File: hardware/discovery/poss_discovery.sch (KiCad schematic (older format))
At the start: 56 parts, among them J1 HEADER_2, J2 HEADER_25x2, J3 HEADER_25x2, J5 HEADER_2, SW1 SW_PUSH, SW10 SW_PUSH, SW11 SW_PUSH, SW12 SW_PUSH, SW13 SW_PUSH, SW14 SW_PUSH, SW15 SW_PUSH, SW16 SW_PUSH, SW17 SW_PUSH, SW18 SW_PUSH, SW19 SW_PUSH, SW2 SW_PUSH, SW20 SW_PUSH, SW21 SW_PUSH, SW22 SW_PUSH, SW3 SW_PUSH, SW4 SW_PUSH, SW5 SW_PUSH, SW6 SW_PUSH, SW7 SW_PUSH, SW8 SW_PUSH, SW9 SW_PUSH

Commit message: Start RevB of the discovery board
- Fix RevA known problems
- Custom scheme and footprint for the headers
- Improved silkscreen
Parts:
- removed J1, J5: HEADER_2, Pin_Headers:Pin_Header_Straight_2x01, symbol HEADER_2
- removed J2, J3: HEADER_25x2, Pin_Headers:Pin_Header_Straight_2x25, symbol HEADER_25x2
- added U1: STM32F4_DISCO_Header, stm32f4-disco:STM32F4-DISCO-HEADERS-TH, symbol STM32F4_DISCO_Header
- RV1, RV2: symbol POT -> POT-RESCUE-poss_discovery
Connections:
- net labels added: BA, BB, BC, BD, BE, BPM_VOL, DISCO_USER_BTN, STM_LED1, SWDCLK, SWDIO, USB_Over_Current, VBUS_FS
- net labels removed: 5V, BOOT0, BP7, BPM, NC, NRTS, PA0, PA1, PA10, PA13, PA14, PA15, PA2, PA3, PA4, PA5, PA6, PA7, PA8, PA9, PB0, PB1, PB10, PB11, PB12, PB13, PB14, PB15, PB2, PB3, PB4, PB5, PB6, PB8, PB9, PC0, PC1, PC10, PC11, PC12, PC13, PC14, PC15, PC2, PC3, PC4, PC5, PC6, PC7, PC8, PC9, PD0, PD1, PD10, PD11, PD12, PD13, PD14, PD15, PD2, PD3, PD4, PD5, PD6, PD7, PD8, PD9, PE0, PE1, PE10, PE11, PE12, PE13, PE14, PE15, PE2, PE3, PE4, PE5, PE6, PE7, PE8, PE9, PH0, PH1, STM_LED_1, STM_USER_BTN, USB_Over_I, VDD, VDD2, Vbus_FS
- wire segments 173 -> 44

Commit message: Discovery: Start power section
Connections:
- net 3V renamed 3V3
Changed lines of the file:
@@
 LIBS:w_connectors
 LIBS:stm32f4_disco_header
+LIBS:74xgxx
+LIBS:ac-dc
+LIBS:brooktre
+LIBS:cmos_ieee
+LIBS:dc-dc
+LIBS:elec-unifil
+LIBS:ftdi
+LIBS:gennum
+LIBS:graphic
+LIBS:logo
+LIBS:microchip_pic10mcu
+LIBS:microchip_pic12mcu
+LIBS:microchip_pic16mcu
+LIBS:microchip1
+LIBS:msp430
+LIBS:nxp_armmcu
+LIBS:powerint
+LIBS:pspice
+LIBS:references
+LIBS:relays
+LIBS:sensors
+LIBS:special
+LIBS:stm8
+LIBS:stm32
+LIBS:supertex
+LIBS:transf
+LIBS:ttl_ieee
+LIBS:video
 LIBS:poss_discovery-cache
 EELAYER 25 0
@@
 $Descr A4 11693 8268
 encoding utf-8
-Sheet 1 1
+Sheet 1 3
 Title "Pocket Open Source Syntesizer - Discovery"
 Date ""
@@
 $EndComp
 Wire Wire Line
-	7400 750  7400 3500
+	7400 750  7400 3750
 Connection ~ 7400 3150
 Connection ~ 7400 2800
@@
 Connection ~ 7400 1100
 Wire Wire Line
-	8650 750  8650 3500
+	8650 750  8650 3750
 Connection ~ 8650 3150
 Connection ~ 8650 2800
@@
 Text GLabel 2200 4950 2    60   Input ~ 0
 GND
-Text GLabel 5350 4950 2    60   Input ~ 0
-GND
 Text GLabel 5350 1350 2    60   Input ~ 0
 GND
@@
 ROW5
 Text GLabel 5350 1650 2    60   Input ~ 0
-3V
+3V3
 Text GLabel 4400 1650 0    60   Input ~ 0
-3V
+3V3
 Text GLabel 3350 5650 2    60   Input ~ 0
 POT1
 Text GLabel 4700 5650 2    60   Input ~ 0
 POT2
-Text GLabel 4950 5900 2    60   Input ~ 0
-GND
-Text GLabel 3600 5900 2    60   Input ~ 0
-GND
 Text GLabel 3100 5900 0    60   Input ~ 0
-3V
+3V3
 Text GLabel 4450 5900 0    60   Input ~ 0
-3V
-Text GLabel 9950 3500 2    60   Input ~ 0
-GND
-Text GLabel 8650 3500 2    60   Input ~ 0
-GND
-Text GLabel 7400 3500 2    60   Input ~ 0
-GND
+3V3
 $Comp
 L GND #PWR01
@@
 Text GLabel 2200 1350 2    60   Input ~ 0
 GND
+$Sheet
+S 1550 6600 1350 1100
+U 585D2CBE
+F0 "Power" 60
+F1 "power.sch" 60
+$EndSheet
+$Comp
+L GND #PWR?
+U 1 1 585D97BE
+P 8650 3750
+F 0 "#PWR?" H 8650 3750 30  0001 C CNN
+F 1 "GND" H 8650 3680 30  0001 C CNN
+F 2 "" H 8650 3750 60  0001 C CNN
+F 3 "" H 8650 3750 60  0001 C CNN
+	1    8650 3750
+	1    0    0    -1
+$EndComp
+Connection ~ 8650 3500
+$Comp
+L GND #PWR?
+U 1 1 585D9E6B
+P 7400 3750
+F 0 "#PWR?" H 7400 3750 30  0001 C CNN
+F 1 "GND" H 7400 3680 30  0001 C CNN
+F 2 "" H 7400 3750 60  0001 C CNN
+F 3 "" H 7400 3750 60  0001 C CNN
+	1    7400 3750
+	1    0    0    -1
+$EndComp
+Connection ~ 7400 3500
+$Comp
+L GND #PWR?
+U 1 1 585DAFE1
+P 4950 6000
+F 0 "#PWR?" H 4950 6000 30  0001 C CNN
+F 1 "GND" H 4950 5930 30  0001 C CNN
+F 2 "" H 4950 6000 60  0001 C CNN
+F 3 "" H 4950 6000 60  0001 C CNN
+	1    4950 6000
+	1    0    0    -1
+$EndComp
+$Comp
+L GND #PWR?
+U 1 1 585DB05F
+P 3600 6000
+F 0 "#PWR?" H 3600 6000 30  0001 C CNN
+F 1 "GND" H 3600 5930 30  0001 C CNN
+F 2 "" H 3600 6000 60  0001 C CNN
+F 3 "" H 3600 6000 60  0001 C CNN
+	1    3600 6000
+	1    0    0    -1
+$EndComp
+Wire Wire Line
+	3600 5900 3600 6000
+Wire Wire Line
+	4950 5900 4950 6000
+Wire Wire Line
+	5350 4950 5500 4950
+Wire Wire Line
+	5500 4950 5500 5100
+Text GLabel 5500 4950 2    60   Input ~ 0
+GND
+$Comp
+L GND #PWR?
+U 1 1 585DBA46
+P 5500 5100
+F 0 "#PWR?" H 5500 5100 30  0001 C CNN
+F 1 "GND" H 5500 5030 30  0001 C CNN
+F 2 "" H 5500 5100 60  0001 C CNN
+F 3 "" H 5500 5100 60  0001 C CNN
+	1    5500 5100
+	1    0    0    -1
+$EndComp
+$Sheet
+S 3200 6600 1400 1100
+U 585DBE08
+F0 "Micro-Controller" 60
+F1 "micro-controller.sch" 60
+$EndSheet
 $EndSCHEMATC

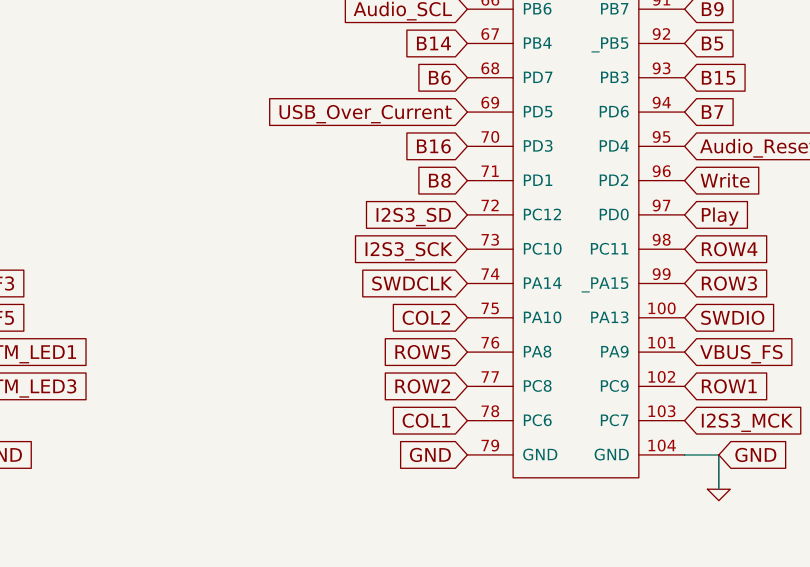
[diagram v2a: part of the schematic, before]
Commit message: Discovery: add the MCU
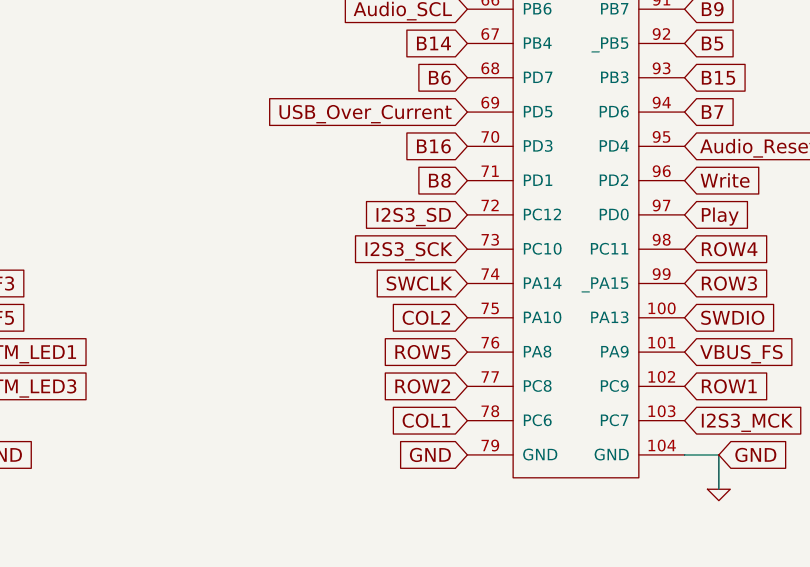
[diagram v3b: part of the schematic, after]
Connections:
- net SWDCLK renamed SWCLK
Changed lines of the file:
@@
 COL2
 Text GLabel 4400 4200 0    60   Input ~ 0
-SWDCLK
+SWCLK
 Text GLabel 4400 4050 0    60   Input ~ 0
 I2S3_SCK

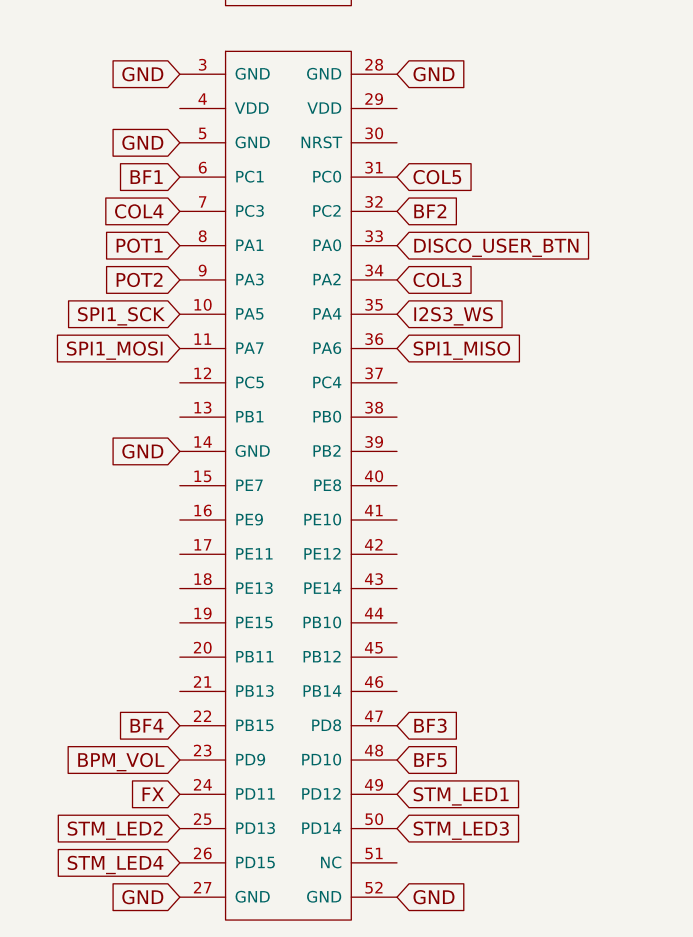
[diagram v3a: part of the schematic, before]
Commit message: Discovery: Fix channel button labels
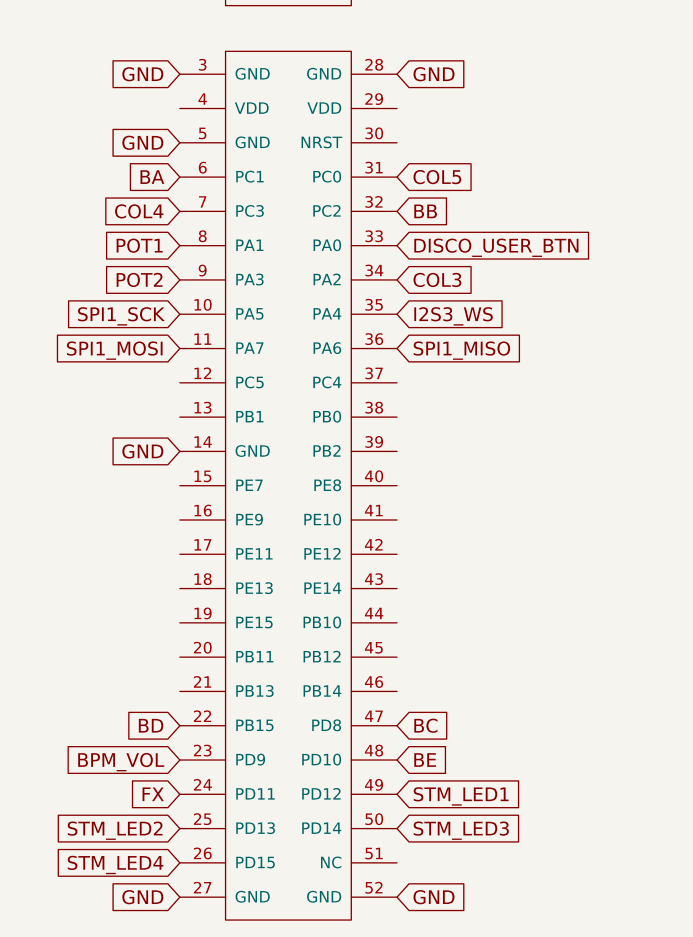
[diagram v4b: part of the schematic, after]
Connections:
- net BF1 is gone; now on net BA: U1.6 (PC1)
- net BF2 is gone; now on net BB: U1.32 (PC2)
- net BF3 is gone; now on net BC: U1.47 (PD8)
- net BF4 is gone; now on net BD: U1.22 (PB15)
- net BF5 is gone; now on net BE: U1.48 (PD10)
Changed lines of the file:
@@
 $EndComp
 Text GLabel 1250 1800 0    60   Input ~ 0
-BF1
+BA
 Text GLabel 1250 1950 0    60   Input ~ 0
 COL4
@@
 COL5
 Text GLabel 2200 1950 2    60   Input ~ 0
-BF2
+BB
 Text GLabel 2200 2100 2    60   Input ~ 0
 DISCO_USER_BTN
@@
 BPM_VOL
 Text GLabel 1250 4200 0    60   Input ~ 0
-BF4
+BD
 Text GLabel 2200 4650 2    60   Input ~ 0
 STM_LED3
@@
 STM_LED1
 Text GLabel 2200 4350 2    60   Input ~ 0
-BF5
+BE
 Text GLabel 2200 4200 2    60   Input ~ 0
-BF3
+BC
 Text GLabel 5350 4800 2    60   Input ~ 0
 I2S3_MCK
@@
 $EndSheet
 $Comp
-L GND #PWR?
+L GND #PWR02
 U 1 1 585D97BE
 P 8650 3750
-F 0 "#PWR?" H 8650 3750 30  0001 C CNN
+F 0 "#PWR02" H 8650 3750 30  0001 C CNN
 F 1 "GND" H 8650 3680 30  0001 C CNN
 F 2 "" H 8650 3750 60  0001 C CNN
@@
 Connection ~ 8650 3500
 $Comp
-L GND #PWR?
+L GND #PWR03
 U 1 1 585D9E6B
 P 7400 3750
-F 0 "#PWR?" H 7400 3750 30  0001 C CNN
+F 0 "#PWR03" H 7400 3750 30  0001 C CNN
 F 1 "GND" H 7400 3680 30  0001 C CNN
 F 2 "" H 7400 3750 60  0001 C CNN
@@
 Connection ~ 7400 3500
 $Comp
-L GND #PWR?
+L GND #PWR04
 U 1 1 585DAFE1
 P 4950 6000
-F 0 "#PWR?" H 4950 6000 30  0001 C CNN
+F 0 "#PWR04" H 4950 6000 30  0001 C CNN
 F 1 "GND" H 4950 5930 30  0001 C CNN
 F 2 "" H 4950 6000 60  0001 C CNN
@@
 $EndComp
 $Comp
-L GND #PWR?
+L GND #PWR05
 U 1 1 585DB05F
 P 3600 6000
-F 0 "#PWR?" H 3600 6000 30  0001 C CNN
+F 0 "#PWR05" H 3600 6000 30  0001 C CNN
 F 1 "GND" H 3600 5930 30  0001 C CNN
 F 2 "" H 3600 6000 60  0001 C CNN
@@
 GND
 $Comp
-L GND #PWR?
+L GND #PWR06
 U 1 1 585DBA46
 P 5500 5100
-F 0 "#PWR?" H 5500 5100 30  0001 C CNN
+F 0 "#PWR06" H 5500 5100 30  0001 C CNN
 F 1 "GND" H 5500 5030 30  0001 C CNN
 F 2 "" H 5500 5100 60  0001 C CNN

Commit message: Discovery start power section
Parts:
- U1: footprint stm32f4-disco:STM32F4-DISCO-HEADERS-TH -> stm32f4-disco:STM32F4-DISCO-HEADERS-SMD
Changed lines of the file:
@@
 LIBS:contrib
 LIBS:valves
-LIBS:w_connectors
 LIBS:stm32f4_disco_header
 LIBS:74xgxx
@@
 F 0 "U1" H 1550 5200 60  0000 C CNN
 F 1 "STM32F4_DISCO_Header" H 2000 5050 60  0000 C CNN
-F 2 "stm32f4-disco:STM32F4-DISCO-HEADERS-TH" H 3350 2900 60  0001 C CNN
+F 2 "stm32f4-disco:STM32F4-DISCO-HEADERS-SMD" H 3350 2900 60  0001 C CNN
 F 3 "" H 3350 2900 60  0001 C CNN
 	1    3350 2900

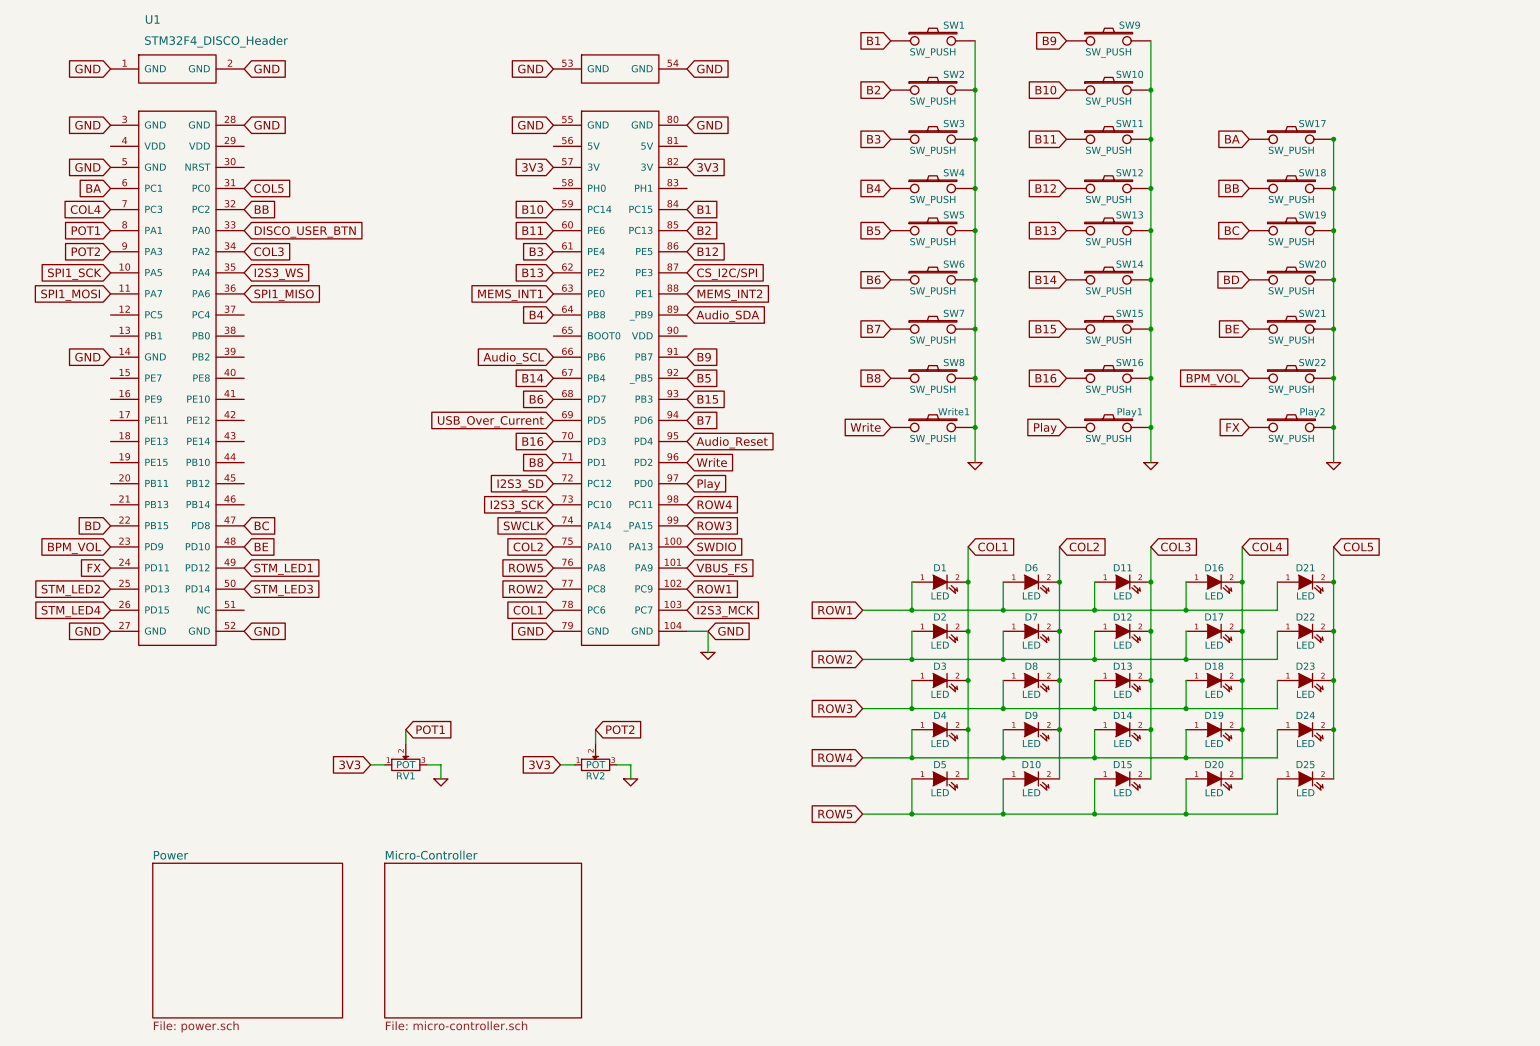
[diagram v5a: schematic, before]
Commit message: Discovery: switch to a 9x3 LED matrix to simplify the PCB layout
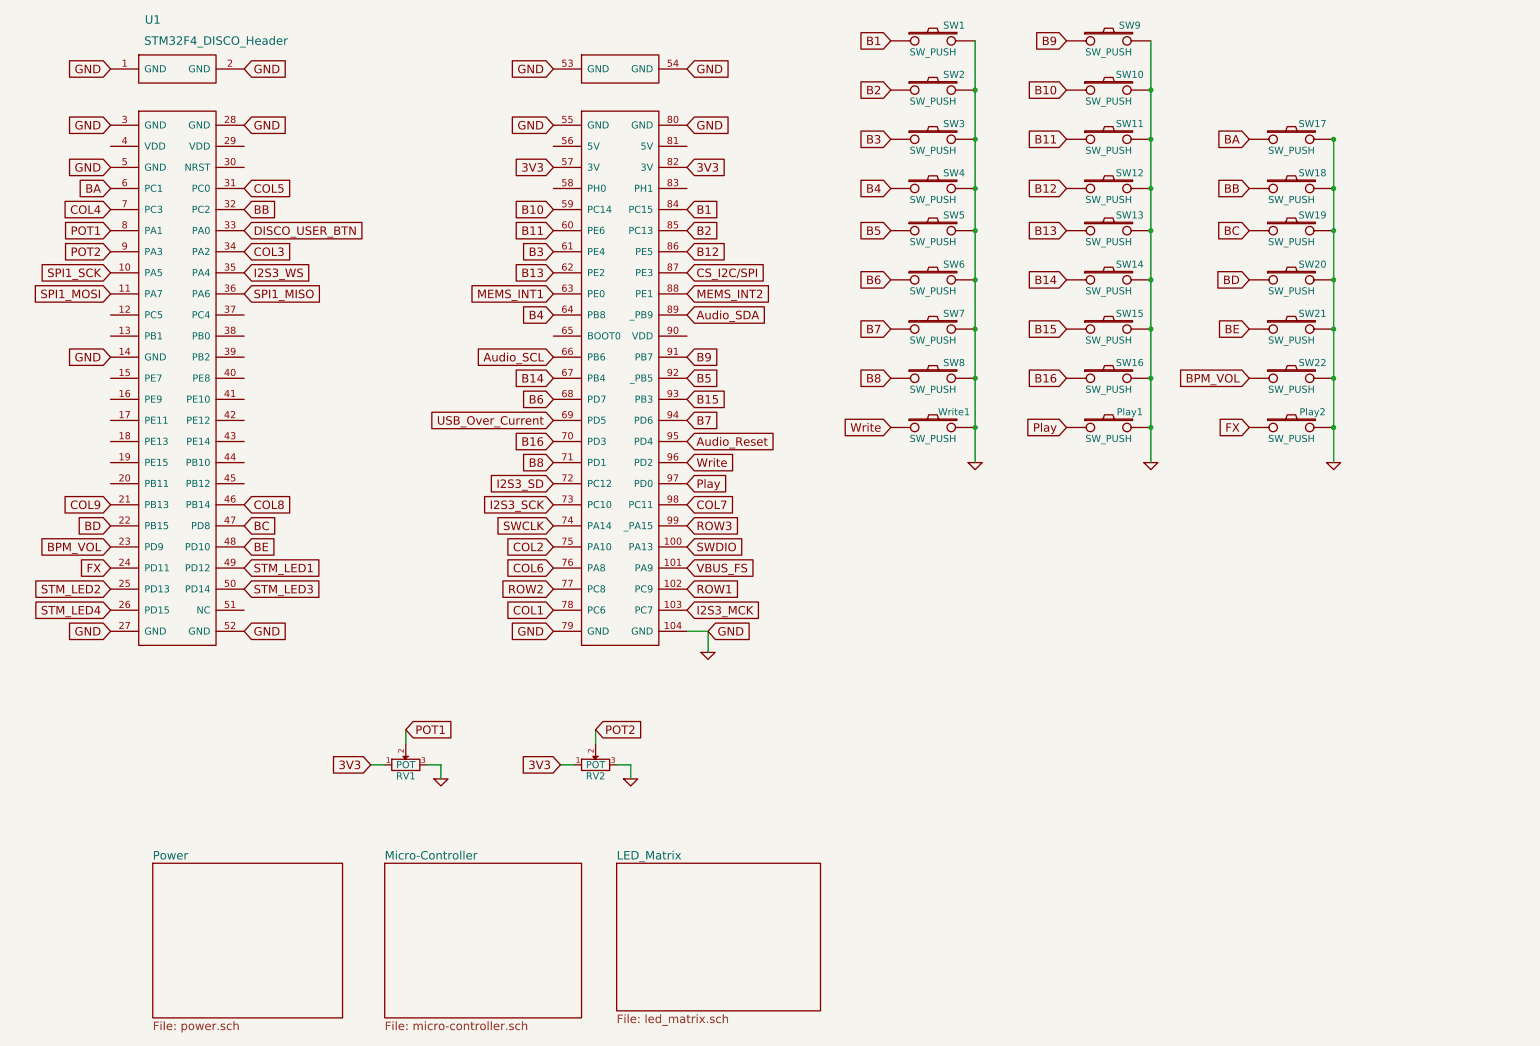
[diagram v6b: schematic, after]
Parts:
- removed D1, D10, D11, D12, D13, D14, D15, D16, D17, D18, D19, D2, D20, D21, D22, D23, D24, D25, D3, D4, D5, D6, D7, D8, D9: LED, LEDs:LED_0805, symbol LED
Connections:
- net COL9: now reaches U1.21 (PB13)
- net COL8: now reaches U1.46 (PB14)
- net ROW4 renamed COL7
- net ROW5 renamed COL6

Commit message: Discovery: Start audio schematic
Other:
- note added: "TODO:\n - Debug port\n - Encoders\n - VBAT sensing\n -"
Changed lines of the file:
@@
 $Descr A4 11693 8268
 encoding utf-8
-Sheet 1 4
+Sheet 1 5
 Title "Pocket Open Source Syntesizer - Discovery"
 Date ""
@@
 Text GLabel 1250 4050 0    60   Input ~ 0
 COL9
+$Sheet
+S 6550 5300 1350 1050
+U 585E4C2D
+F0 "Audio" 60
+F1 "audio.sch" 60
+$EndSheet
+Text Notes 9000 5500 0    157  ~ 0
+TODO:\n - Debug port\n - Encoders\n - VBAT sensing\n -
+Wire Notes Line
+	11150 4100 8850 4100
+Wire Notes Line
+	8850 4100 8850 6450
 $EndSCHEMATC
